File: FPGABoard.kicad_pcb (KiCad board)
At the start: 2 copper layers, 100 x 80 mm, 87 parts, among them P1 JTAG_FPGA, P2 CONN_02X03, P3 USB_B, P4 CONN_02X07, P5 JTAG, P6 CONN_02X07, P7 CONN_02X07, P8 CONN_02X07, Q1 Q_NMOS_DSG, SW1 SW_PUSH, SW2 SW_PUSH, U1 XC3S50A/VQ100, U2 LM317_SOT223, U3 LM317_SOT223, U4 LM317_SOT223, U5 ATMEGA32U4RC-A, U6 M25P20, U7 XO53, Y1 12MHz

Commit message: Ready for Production
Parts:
- removed GS1, GS2, GS3: VS, Connect:GS2
- removed R2: 330R, Resistors_SMD:R_0805_HandSoldering
- removed the REF*** at (101.6, 135.3)
- removed S1: MO, Buttons_Switches_ThroughHole:SW_DIP_x3_Slide
- added C37: 10µF, Capacitors_SMD:C_0805_HandSoldering, B.Cu at (105.8, 75.8)
- added C38: 10µF, Capacitors_SMD:C_0805_HandSoldering, B.Cu at (111.1, 120.4)
- added C39: 10µF, Capacitors_SMD:C_0805_HandSoldering, B.Cu at (125.2, 120.4)
- added D10: ZD3.6, Diodes_SMD:D_SOT-23_ANK, B.Cu at (174.2, 107.7)
- added D11: ZD3.6, Diodes_SMD:D_SOT-23_ANK, B.Cu at (170.2, 83.2)
- added D12: ZD3.6, Diodes_SMD:D_SOT-23_ANK, B.Cu at (101.9, 101.9)
- added D13: ZD3.6, Diodes_SMD:D_SOT-23_ANK, B.Cu at (105.9, 127.0)
- added D8: ES1DL, w_smd_diode:sod323, B.Cu at (115.3, 75.9)
- added D9: ES1DL, w_smd_diode:sod323, B.Cu at (107.8, 81.3)
- added R19: 1k, Resistors_SMD:R_0805_HandSoldering, B.Cu at (111.9, 134.5)
- added R20: 1k, Resistors_SMD:R_0805_HandSoldering, B.Cu at (126.6, 134.5)
- added REF***: OSHW-Logo2_9.8x8mm_SilkScreen, Symbols:OSHW-Logo2_9.8x8mm_SilkScreen, F.Cu at (171.7, 134.1)
- added SW3: SW_Push, SMD_Switch_LSX1301:SW_LSx_1301, F.Cu at (137.8, 86.4)
- added SW4: SW_DIP_x02, w_switch:dip_2-300, F.Cu at (166.4, 108.6)
- C26, C27: value 22pF -> 12pF
- C30: moved to F.Cu
- C31, R3: moved to B.Cu
- D1: value LED_DONE -> Green
- D2: value LED_PWR -> Green
- D3: value LED_STATUS -> Yellow
- D4: value LED_USB -> Yellow
- D5, D6, D7: value LED -> Green
- P2: value CONN_02X03 -> UART; footprint Pin_Headers:Pin_Header_Straight_2x03 -> Pin_Headers:Pin_Header_Straight_1x03_Pitch2.54mm
- Q1: value Q_NMOS_DSG -> BSS123
- R10: value 10R -> 1R
- R13, R14, R15, R16, R17, R7: value 100R -> 36R
- R18: value 100R -> 36R; moved to F.Cu
- U7: value XO53 -> 50MHz
- Y1: value 12MHz -> 16MHz
- moved G*** 96.8 mm to (93.3, 71.8)
- moved C31 59.9 mm to (111.8, 74.4), turned to 180 degrees
- moved R3 58.1 mm to (123.4, 94.0), turned to 270 degrees
- moved C30 49.0 mm to (170.7, 64.5), turned to 90 degrees
- moved R11 37.9 mm to (111.8, 76.8)
- moved R12 37.9 mm to (111.8, 74.3)
- moved P3 34.7 mm to (104.8, 65.4)
- moved C15 27.9 mm to (114.9, 67.3), turned to 270 degrees
- moved C17 26.0 mm to (134.1, 96.8), turned to 135 degrees
- moved D4 21.8 mm to (140.1, 67.1), turned to 90 degrees
- moved D2 21.7 mm to (125.3, 67.1), turned to 90 degrees
- moved D1 21.7 mm to (147.6, 67.1), turned to 270 degrees
- moved D3 21.7 mm to (133.0, 67.1), turned to 90 degrees
- moved R16 21.6 mm to (147.6, 67.1)
- moved R13 21.6 mm to (133.0, 67.1)
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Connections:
- net Net-(D3-Pad2) renamed /Microcontroller/LED_STATUS
- net Net-(D4-Pad2) renamed /Microcontroller/LED_USB
- net Net-(P5-Pad1) renamed /Microcontroller/TCK
- net Net-(P5-Pad3) renamed /Microcontroller/TDO
- net Net-(P5-Pad5) renamed /Microcontroller/TMS
- net Net-(P5-Pad9) renamed /Microcontroller/TDI
- C18 pad 1: VCC -> /Microcontroller/V_USB
- P2 pad 1: VCC -> /Microcontroller/RXD
- P2 pad 2: GND -> /Microcontroller/TXD
- P2 pad 3: /Connections/C_IO1 -> GND
- Q1 pad 1: Net-(D1-Pad1) -> /Microcontroller/DONE
- Q1 pad 3: /Microcontroller/DONE -> Net-(D1-Pad1)
- R3 pad 1: VCC -> /Microcontroller/INIT_B
- R3 pad 2: /Microcontroller/INIT_B -> VCC_AUX
- U1 pad 23: Net-(S1-Pad2) -> /Spartan3A/M1
- U1 pad 24: Net-(S1-Pad3) -> /Spartan3A/M2
- U1 pad 25: Net-(S1-Pad1) -> (no net)
- U1 pad 29: Net-(GS3-Pad2) -> (no net)
- U1 pad 30: Net-(GS1-Pad2) -> (no net)
- U1 pad 31: Net-(GS2-Pad2) -> (no net)
- U3 pad 3: VCC -> /Microcontroller/V_USB
- U5 pad 18: /Connections/C_IO2 -> (no net)
- U5 pad 19: /Connections/C_IO3 -> (no net)
- U5 pad 20: (no net) -> /Microcontroller/RXD
- U5 pad 21: /Microcontroller/MOSI -> /Microcontroller/TXD
- U5 pad 22: /Microcontroller/SCK -> (no net)
- U5 pad 25: /Connections/C_IO4 -> (no net)
- U5 pad 31: /Connections/C_IO1 -> (no net)
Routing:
- net /Microcontroller/V_USB: track 62.5 -> 190.2 mm
- net VCC: track 458.8 -> 408.5 mm, vias 14 -> 17
- net /Microcontroller/PROG_B: track 75.1 -> 119.1 mm, vias 3 -> 5
- net Net-(S1-Pad1): track 41.8 -> 0.00 mm, vias 1 -> 0
- net /Microcontroller/D-: track 8.57 -> 47.8 mm
- net /Microcontroller/D+: track 8.61 -> 47.8 mm
- net Net-(S1-Pad2): track 38.5 -> 0.00 mm, vias 1 -> 0
- net /Spartan3A/M2: track 0.00 -> 37.8 mm, vias 0 -> 1
- net GND: track 266.6 -> 303.1 mm, vias 72 -> 77
- net Net-(S1-Pad3): track 35.1 -> 0.00 mm, vias 1 -> 0
- net /Spartan3A/M1: track 0.00 -> 34.2 mm, vias 0 -> 1
- net /Microcontroller/TDO: track 71.6 -> 43.5 mm, vias 0 -> 1
- net /Microcontroller/RXD: track 0.00 -> 25.6 mm
- net Net-(D1-Pad1): track 53.4 -> 28.4 mm
- net /Connections/C_IO3: track 23.8 -> 0.00 mm, vias 1 -> 0
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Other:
- board text added: "FPGA Reset"
- board text added: "GND"
- board text added: "LED"
- board text added: "Prog. Mode"
- board text added: "RX"
- board text added: "TX"
- board text removed: "Debug"
- board text removed: "LV 0"
- board text removed: "LV 1"
- board text removed: "LV 2"
- board text removed: "Progr. Mode"
- board text removed: "Spartan 3A Eval-Board"

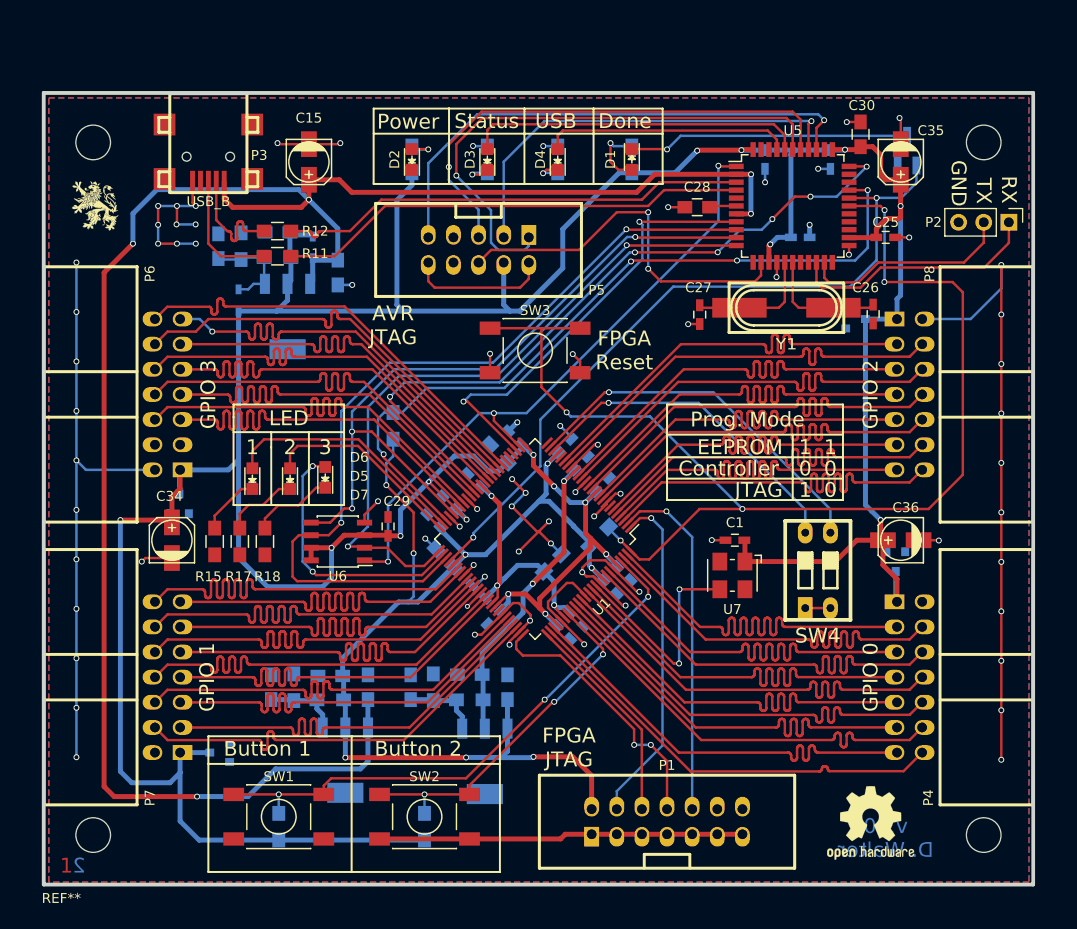
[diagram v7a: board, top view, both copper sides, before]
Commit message: Changed SPI Connection to support Multi-Master
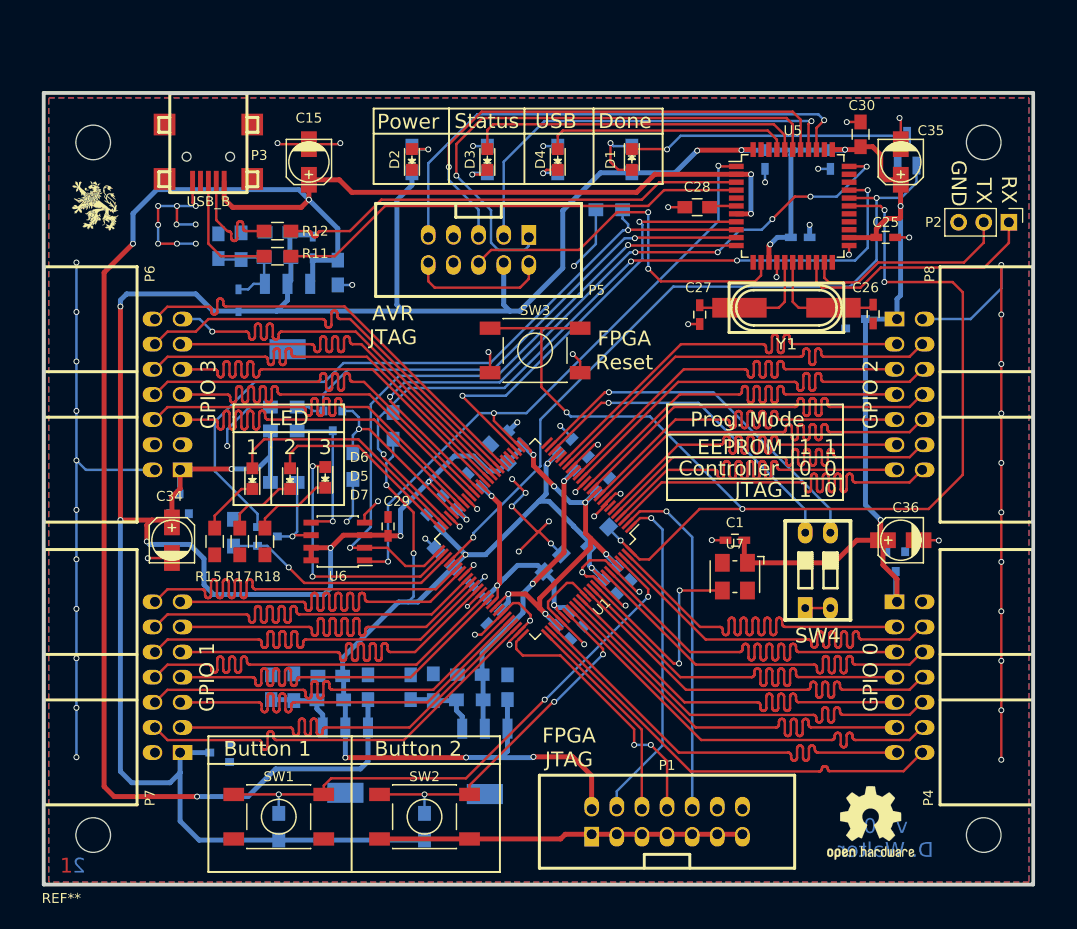
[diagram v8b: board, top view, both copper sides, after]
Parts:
- added D14: BAT54A, TO_SOT_Packages_SMD:SOT-23, B.Cu at (117.3, 93.5)
- added D15: BAT54A, TO_SOT_Packages_SMD:SOT-23, B.Cu at (110.7, 105.2)
- added R2: 330R, Resistors_SMD:R_0805_HandSoldering, B.Cu at (112.4, 94.5)
- added R21: 15k, Resistors_SMD:R_0805_HandSoldering, B.Cu at (119.4, 98.0)
- added R22: 330R, Resistors_SMD:R_0805_HandSoldering, B.Cu at (112.4, 99.7)
- added R23: 15k, Resistors_SMD:R_0805_HandSoldering, B.Cu at (107.3, 104.8)
- added R24: 15k, Resistors_SMD:R_0805_HandSoldering, B.Cu at (112.4, 92.1)
- added R25: 15k, Resistors_SMD:R_0805_HandSoldering, B.Cu at (145.3, 72.1)
- moved U7 0.28 mm to (158.0, 109.2)
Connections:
- net /Microcontroller/MISO renamed /Microcontroller/MISO_C
- U1 pad 46: /Microcontroller/MOSI -> /Spartan3A/MOSI_F
- U1 pad 53: /Microcontroller/SCK -> /Spartan3A/SCK_F
- U5 pad 10: /Microcontroller/MOSI -> /Microcontroller/MOSI_C
- U5 pad 9: /Microcontroller/SCK -> /Microcontroller/SCK_C
- U6 pad 5: /Microcontroller/MOSI -> /Spartan3A/MOSI
- U6 pad 6: /Microcontroller/SCK -> /Spartan3A/SCK
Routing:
- net /Microcontroller/SCK: track 84.8 -> 0.00 mm, vias 2 -> 0
- net /Microcontroller/SCK_C: track 0.00 -> 75.5 mm, vias 0 -> 1
- net /Microcontroller/MOSI: track 74.4 -> 0.00 mm, vias 3 -> 0
- net /Microcontroller/MOSI_C: track 0.00 -> 52.8 mm, vias 0 -> 1
- net VCC: track 408.5 -> 443.5 mm, vias 17 -> 20
- net /Spartan3A/SCK_F: track 0.00 -> 24.2 mm, vias 0 -> 1
- net /Spartan3A/MOSI_F: track 0.00 -> 18.8 mm, vias 0 -> 1
- net GND: track 303.1 -> 320.7 mm, vias 77 -> 80
- net /Spartan3A/MOSI: track 0.00 -> 15.0 mm, vias 0 -> 1
- net /Spartan3A/SCK: track 0.00 -> 9.12 mm, vias 0 -> 1
- net /Microcontroller/INIT_B: track 77.5 -> 78.0 mm
